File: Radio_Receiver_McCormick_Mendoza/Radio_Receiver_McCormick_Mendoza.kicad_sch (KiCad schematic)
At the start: 0 parts

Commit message: slight updates to the KiCad files
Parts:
- added U1: RP2040, Package_DFN_QFN:QFN-56-1EP_7x7mm_P0.4mm_EP3.2x3.2mm, symbol MCU_RaspberryPi:RP2040
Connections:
- new net: U1.1 (IOVDD), U1.10 (IOVDD), U1.22 (IOVDD), U1.33 (IOVDD), U1.42 (IOVDD), U1.49 (IOVDD)
- new net: U1.23 (DVDD), U1.50 (DVDD)
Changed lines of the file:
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@@
 		(comment 3 "Jeffrey McCormick")
+	)
+	(symbol
+		(lib_id "MCU_RaspberryPi:RP2040")
+		(at 80.01 69.85 0)
+		(unit 1)
+		(body_style 1)
+		(exclude_from_sim no)
+		(in_bom yes)
+		(on_board yes)
+		(in_pos_files yes)
+		(dnp no)
+		(fields_autoplaced yes)
+		(property "Reference" "U1"
+			(at 82.1533 114.3 0)
+			(show_name no)
+			(do_not_autoplace no)
+			(effects
+				(font
+					(size 1.27 1.27)
+				)
+				(justify left)
+			)
+		)
+		(property "Value" "RP2040"
+			(at 82.1533 116.84 0)
+			(show_name no)
+			(do_not_autoplace no)
+			(effects
+				(font
+					(size 1.27 1.27)
+				)
+				(justify left)
+			)
+		)
+		(property "Footprint" "Package_DFN_QFN:QFN-56-1EP_7x7mm_P0.4mm_EP3.2x3.2mm"
+			(at 80.01 69.85 0)
+			(hide yes)
+			(show_name no)
+			(do_not_autoplace no)
+			(effects
+				(font
+					(size 1.27 1.27)
+				)
+			)
+		)
+		(property "Datasheet" "https://datasheets.raspberrypi.com/rp2040/rp2040-datasheet.pdf"
+			(at 80.01 69.85 0)
+			(hide yes)
+			(show_name no)
+			(do_not_autoplace no)
+			(effects
+				(font
+					(size 1.27 1.27)
+				)
+			)
+		)
+		(property "Description" "A microcontroller by Raspberry Pi, Dual ARM Cortex-M0+, 133MHz, no flash, 264KB SRAM, 8 PIO state machines, VQFN-56"
+			(at 80.01 69.85 0)
+			(hide yes)
+			(show_name no)
+			(do_not_autoplace no)
+			(effects
+				(font
+					(size 1.27 1.27)
+				)
+			)
+		)
+		(property private "KLC_S4.2_DVDD" "Not a standalone power converter; internal on-chip voltage regulator for digital core supply; DVDD is the digital core power supply, should be placed next to voltage regulator output."
+			(at 80.01 72.39 0)
+			(hide yes)
+			(show_name yes)
+			(do_not_autoplace no)
+			(effects
+				(font
+					(size 1.27 1.27)
+				)
+			)
+		)
+		(property private "KLC_S4.2_VREG_VOUT" "Should be placed next to DVDD."
+			(at 80.01 72.39 0)
+			(hide yes)
+			(show_name yes)
+			(do_not_autoplace no)
+			(effects
+				(font
+					(size 1.27 1.27)
+				)
+			)
+		)
+		(pin "1"
+		)
+		(pin "3"
+		)
+		(pin "14"
+		)
+		(pin "10"
+		)
+		(pin "20"
+		)
+		(pin "23"
+		)
+		(pin "16"
+		)
+		(pin "27"
+		)
+		(pin "29"
+		)
+		(pin "21"
+		)
+		(pin "34"
+		)
+		(pin "26"
+		)
+		(pin "31"
+		)
+		(pin "19"
+		)
+		(pin "32"
+		)
+		(pin "17"
+		)
+		(pin "4"
+		)
+		(pin "5"
+		)
+		(pin "2"
+		)
+		(pin "6"
+		)
+		(pin "9"
+		)
+		(pin "13"
+		)
+		(pin "12"
+		)
+		(pin "8"
+		)
+		(pin "11"
+		)
+		(pin "7"
+		)
+		(pin "15"
+		)
+		(pin "18"
+		)
+		(pin "22"
+		)
+		(pin "24"
+		)
+		(pin "25"
+		)
+		(pin "28"
+		)
+		(pin "30"
+		)
+		(pin "33"
+		)
+		(pin "44"
+		)
+		(pin "42"
+		)
+		(pin "51"
+		)
+		(pin "39"
+		)
+		(pin "43"
+		)
+		(pin "45"
+		)
+		(pin "40"
+		)
+		(pin "35"
+		)
+		(pin "41"
+		)
+		(pin "48"
+		)
+		(pin "49"
+		)
+		(pin "56"
+		)
+		(pin "36"
+		)
+		(pin "47"
+		)
+		(pin "50"
+		)
+		(pin "37"
+		)
+		(pin "46"
+		)
+		(pin "55"
+		)
+		(pin "38"
+		)
+		(pin "57"
+		)
+		(pin "52"
+		)
+		(pin "53"
+		)
+		(pin "54"
+		)
+		(instances
+			(project "Radio_Receiver_McCormick_Mendoza"
+				(path "/f31d31ab-6846-4f3a-92b1-aa5a6a13373f"
+					(reference "U1")
+					(unit 1)
+				)
+			)
+		)
 	)
 	(sheet

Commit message: Added Bibliography entry
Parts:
- added C6: 0.1uF, symbol Device:C
- added J7: Conn_02x03_Counter_Clockwise, symbol Connector_Generic:Conn_02x03_Counter_Clockwise
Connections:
- net +3.3V: now reaches U1.1 (IOVDD), U1.10 (IOVDD), U1.22 (IOVDD), U1.33 (IOVDD), U1.42 (IOVDD), U1.49 (IOVDD)
- net +3.3V: now also C6.1, J7.5 (Pin_5)
- net SWCLK: now reaches U1.24 (SWCLK)
- net SWCLK: now also J7.2 (Pin_2)
- net SWDIO: now reaches U1.25 (SWDIO)
- net SWDIO: now also J7.1 (Pin_1)
- net ~{SWRESET}: now reaches U1.26 (RUN)
- net ~{SWRESET}: now also J7.6 (Pin_6)
- net GND: now reaches U1.57 (GND)
- net GND: now also C6.2, J7.3 (Pin_3), J7.4 (Pin_4)
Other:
- note added: "YD-RP2040 Programming Header"
- moved on the sheet: U1

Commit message: Added switchable antenna filters and photos.
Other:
- added sheet ADC-24bit (ADC-24bit.kicad_sch)
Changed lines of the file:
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@@
+	)
+	(sheet
+		(at 259.715 134.62)
+		(size 12.7 7.62)
+		(exclude_from_sim no)
+		(in_bom yes)
+		(on_board yes)
+		(dnp no)
+		(fields_autoplaced yes)
+		(stroke
+			(width 0.1524)
+			(type solid)
+		)
+		(fill
+			(color 0 0 0 0)
+		)
+		(property "Sheetname" "ADC-24bit"
+			(at 259.715 133.9084 0)
+			(show_name no)
+			(do_not_autoplace no)
+			(effects
+				(font
+					(size 1.27 1.27)
+				)
+				(justify left bottom)
+			)
+		)
+		(property "Sheetfile" "ADC-24bit.kicad_sch"
+			(at 259.715 142.8246 0)
+			(show_name no)
+			(do_not_autoplace no)
+			(effects
+				(font
+					(size 1.27 1.27)
+				)
+				(justify left top)
+			)
+		)
+		(instances
+			(project "Radio_Receiver_McCormick_Mendoza"
+				(path "/f31d31ab-6846-4f3a-92b1-aa5a6a13373f"
+					(page "9")
+				)
+			)
+		)
 	)
 	(sheet

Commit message: Schematic edits power and signal systems
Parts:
- removed C6: 0.1uF, symbol Device:C
- removed J7: Conn_02x03_Counter_Clockwise, symbol Connector_Generic:Conn_02x03_Counter_Clockwise
- removed U1: RP2040, Package_DFN_QFN:QFN-56-1EP_7x7mm_P0.4mm_EP3.2x3.2mm, symbol MCU_RaspberryPi:RP2040
- added R22, R23: 4.7kΩ, PCM_JLCPCB:R_0805, symbol PCM_JLCPCB-Resistors:0805,4.7kΩ
- added R24, R25, R26, R27: 100Ω, PCM_JLCPCB:R_0805, symbol PCM_JLCPCB-Resistors:0805,100Ω
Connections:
- net +3.3V: now also R22.1, R23.1
- new net OSC_SCL: R25.1
- new net OSC_SDA: R24.1
- new net Raspberry_Pi_Pico/GPIO12: R22.2, R24.2, R27.2
- new net Raspberry_Pi_Pico/GPIO13: R23.2, R25.2, R26.2
- new net SCL: R26.1
- new net SDA: R27.1
- no-connect marks 0 -> 3
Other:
- removed sheet Low-Pass Filter
- removed sheet RP-2040
- added sheet Raspberry_Pi_Pico (raspberry_pi_pico.kicad_sch)
- note added: "I2C"
- note added: "USB"
- note removed: "YD-RP2040 Programming Header"

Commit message: Added reference voltage stability by buffer amp
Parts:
- added C13: 100nF, PCM_JLCPCB:C_0402, symbol PCM_JLCPCB-Capacitors:0402,100nF
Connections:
- net +3.3V: now also C13.1
- new net GND: C13.2

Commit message: Isolated filter switching MUX from digital control
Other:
- note added: "To control the filter type"
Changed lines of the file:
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@@
+		)
+	)
+	(text "To control the\nfilter type"
+		(exclude_from_sim no)
+		(at 128.524 80.264 0)
+		(effects
+			(font
+				(size 1.27 1.27)
+			)
 		)
 	)
@@
 		)
 	)
+	(global_label "CTL1"
+		(shape output)
+		(at 114.3 77.47 0)
+		(fields_autoplaced yes)
+		(effects
+			(font
+				(size 1.27 1.27)
+			)
+			(justify left)
+		)
+		(property "Intersheetrefs" "${INTERSHEET_REFS}"
+			(at 121.7604 77.47 0)
+			(hide yes)
+			(show_name no)
+			(do_not_autoplace no)
+			(effects
+				(font
+					(size 1.27 1.27)
+				)
+				(justify left)
+			)
+		)
+	)
+	(global_label "CTL2"
+		(shape output)
+		(at 114.3 82.55 0)
+		(fields_autoplaced yes)
+		(effects
+			(font
+				(size 1.27 1.27)
+			)
+			(justify left)
+		)
+		(property "Intersheetrefs" "${INTERSHEET_REFS}"
+			(at 121.7604 82.55 0)
+			(hide yes)
+			(show_name no)
+			(do_not_autoplace no)
+			(effects
+				(font
+					(size 1.27 1.27)
+				)
+				(justify left)
+			)
+		)
+	)

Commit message: Added DAC and shaft angle encoder
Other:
- added sheet Angle Encoder (Angle_Encoder.kicad_sch)
- added sheet Audio DAC (Audio_DAC.kicad_sch)
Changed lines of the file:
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@@
+	)
+	(sheet
+		(at 179.07 36.83)
+		(size 12.7 7.62)
+		(exclude_from_sim no)
+		(in_bom yes)
+		(on_board yes)
+		(dnp no)
+		(fields_autoplaced yes)
+		(stroke
+			(width 0.1524)
+			(type solid)
+		)
+		(fill
+			(color 0 0 0 0)
+		)
+		(property "Sheetname" "Angle Encoder"
+			(at 179.07 36.1184 0)
+			(show_name no)
+			(do_not_autoplace no)
+			(effects
+				(font
+					(size 1.27 1.27)
+				)
+				(justify left bottom)
+			)
+		)
+		(property "Sheetfile" "Angle_Encoder.kicad_sch"
+			(at 179.07 45.0346 0)
+			(show_name no)
+			(do_not_autoplace no)
+			(effects
+				(font
+					(size 1.27 1.27)
+				)
+				(justify left top)
+			)
+		)
+		(instances
+			(project "Radio_Receiver_McCormick_Mendoza"
+				(path "/f31d31ab-6846-4f3a-92b1-aa5a6a13373f"
+					(page "10")
+				)
+			)
+		)
 	)
 	(sheet
@@
 				)
 			)
+		)
+	)
+	(sheet
+		(at 225.425 38.735)
+		(size 12.7 7.62)
+		(exclude_from_sim no)
+		(in_bom yes)
+		(on_board yes)
+		(dnp no)
+		(fields_autoplaced yes)
+		(stroke
+			(width 0.1524)
+			(type solid)
+		)
+		(fill
+			(color 0 0 0 0)
+		)
+		(property "Sheetname" "Audio DAC"
+			(at 225.425 38.0234 0)
+			(show_name no)
+			(do_not_autoplace no)
+			(effects
+				(font
+					(size 1.27 1.27)
+				)
+				(justify left bottom)
+			)
+		)
+		(property "Sheetfile" "Audio_DAC.kicad_sch"
+			(at 225.425 46.9396 0)
+			(show_name no)
+			(do_not_autoplace no)
+			(effects
+				(font
+					(size 1.27 1.27)
+				)
+				(justify left top)
+			)
+		)
+		(instances
+			(project "Radio_Receiver_McCormick_Mendoza"
+				(path "/f31d31ab-6846-4f3a-92b1-aa5a6a13373f"
+					(page "9")
+				)
+			)

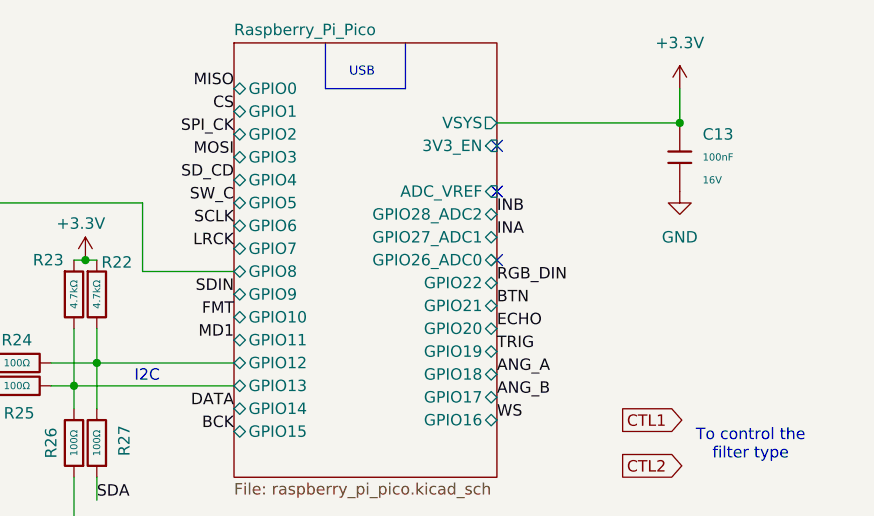
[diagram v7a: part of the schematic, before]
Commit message: Added digital power regulator
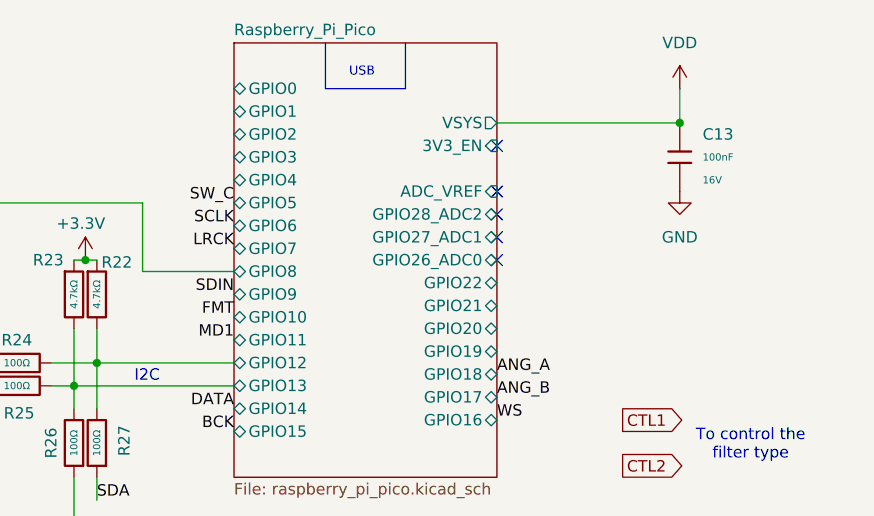
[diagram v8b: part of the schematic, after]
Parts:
- C13: Manufacturer Samsung Electro-Mechanics -> (none)
- R22, R23, R24, R25, R26, R27: Manufacturer UNI-ROYAL(Uniroyal Elec) -> (none)
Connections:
- net +3.3V: no longer C13.1
- new net VDD: C13.1
- no-connect marks 3 -> 5
